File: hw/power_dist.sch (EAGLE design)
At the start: 78 parts, among them J1 JST-ZH6SMT_VERT, J2 JST-PH4SMT_VERT, J3 JST-PH5VERT, P1 XT30P, P2 XT30P, P3 XT30P, P4 XT30P, P5 XT30P, P6 XT30P, P7 XT90PW-M, Q1 PSMN4R8-100BSEJ, Q2 PSMN4R8-100BSEJ, Q3 PSMN4R8-100BSEJ, Q4 MF-DSC-SOT233-MMBT3904, Q5 MMBT5401 100V, U1 MAX15062AATA+T, U2 STM32G474CEU6, U4 TCAN334G, U5 LT1787HVIMS8PBF, U6 LTC4830, X3 FSV10150VTO277-3L_ONS-L

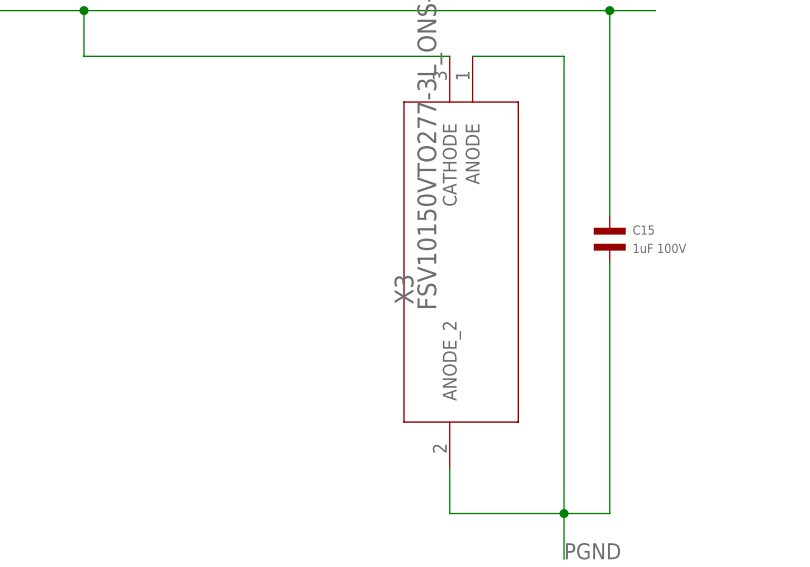
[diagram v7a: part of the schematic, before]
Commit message: Fix more minor layout and naming glitches
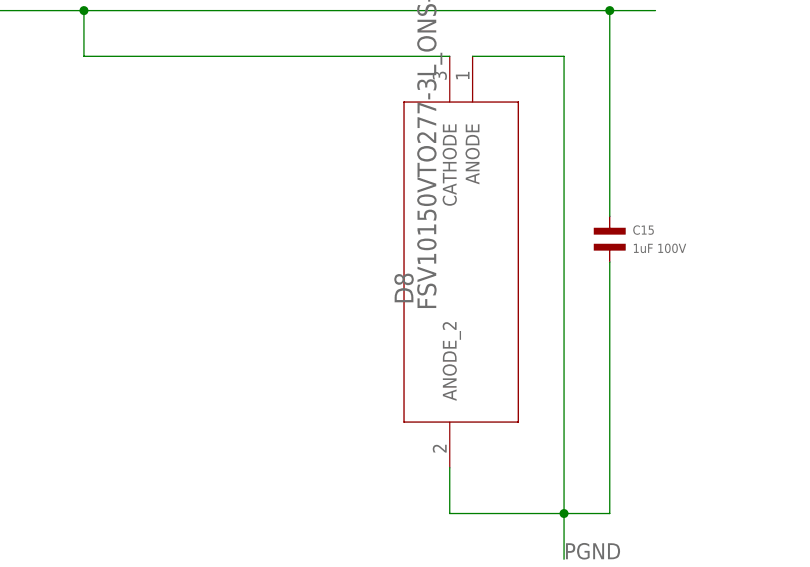
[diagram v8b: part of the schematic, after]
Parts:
- renumbered X3 to D8
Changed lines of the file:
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@@
 <attribute name="POPULATE" value="1"/>
 </part>
-<part name="X3" library="power_dist" deviceset="FSV10150V" device="TO277-3L_ONS-L" value="FSV10150VTO277-3L_ONS-L">
+<part name="D8" library="power_dist" deviceset="FSV10150V" device="TO277-3L_ONS-L" value="FSV10150VTO277-3L_ONS-L">
 <attribute name="MPN" value="FSV10150V"/>
 <attribute name="POPULATE" value="1"/>
@@
 <attribute name="POPULATE" x="-63.5" y="7.62" size="1.778" layer="96" rot="R90" display="off"/>
 </instance>
-<instance part="X3" gate="A" x="83.82" y="-25.4" smashed="yes" rot="R90">
+<instance part="D8" gate="A" x="83.82" y="-25.4" smashed="yes" rot="R90">
 <attribute name="NAME" x="79.7814" y="-4.7244" size="2.0828" layer="95" ratio="6" rot="SR90"/>
 <attribute name="VALUE" x="82.3214" y="-5.3594" size="2.0828" layer="96" ratio="6" rot="SR90"/>
@@
 <segment>
 <label x="43.18" y="30.48" size="1.778" layer="95"/>
-<pinref part="X3" gate="A" pin="CATHODE"/>
+<pinref part="D8" gate="A" pin="CATHODE"/>
 <wire x1="83.82" y1="22.86" x2="43.18" y2="22.86" width="0.1524" layer="91"/>
 <wire x1="43.18" y1="22.86" x2="43.18" y2="27.94" width="0.1524" layer="91"/>
@@
 </segment>
 <segment>
-<pinref part="X3" gate="A" pin="ANODE"/>
+<pinref part="D3" gate="A" pin="2"/>
+<wire x1="-63.5" y1="7.62" x2="-63.5" y2="0" width="0.1524" layer="91"/>
+<label x="-66.04" y="-2.54" size="1.778" layer="95"/>
+</segment>
+<segment>
+<pinref part="D8" gate="A" pin="ANODE"/>
 <wire x1="86.36" y1="22.86" x2="96.52" y2="22.86" width="0.1524" layer="91"/>
 <wire x1="96.52" y1="22.86" x2="96.52" y2="-27.94" width="0.1524" layer="91"/>
-<pinref part="X3" gate="A" pin="ANODE_2"/>
+<pinref part="D8" gate="A" pin="ANODE_2"/>
 <wire x1="96.52" y1="-27.94" x2="96.52" y2="-33.02" width="0.1524" layer="91"/>
 <wire x1="83.82" y1="-22.86" x2="83.82" y2="-27.94" width="0.1524" layer="91"/>
@@
 <label x="96.52" y="-33.02" size="1.778" layer="95"/>
 </segment>
-<segment>
-<pinref part="D3" gate="A" pin="2"/>
-<wire x1="-63.5" y1="7.62" x2="-63.5" y2="0" width="0.1524" layer="91"/>
-<label x="-66.04" y="-2.54" size="1.778" layer="95"/>
-</segment>
-</net>
+</net>
